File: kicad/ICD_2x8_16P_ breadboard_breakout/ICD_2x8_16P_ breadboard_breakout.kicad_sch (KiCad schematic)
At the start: 3 parts, among them J1 Conn_02x08_Top_Bottom, J2 Conn_01x08, J3 Conn_01x08

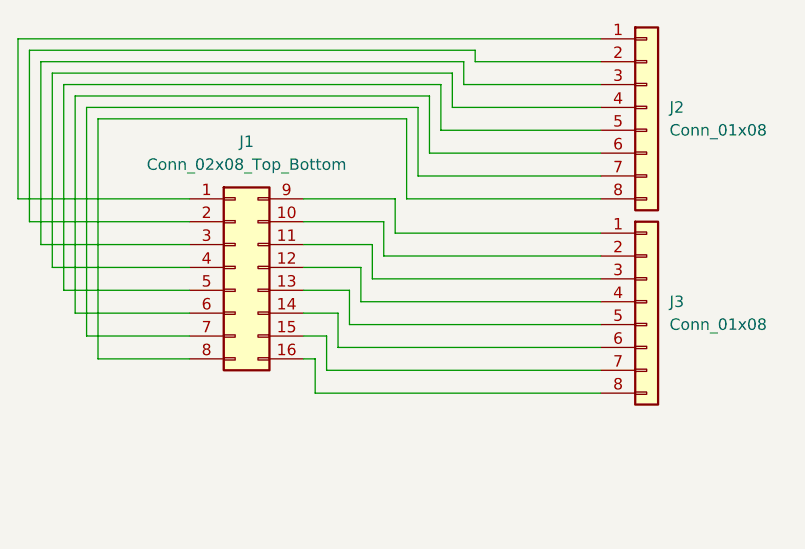
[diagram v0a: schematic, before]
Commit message: Major progress on Serial, KiCAD models, and Python libraries for sensor module base.
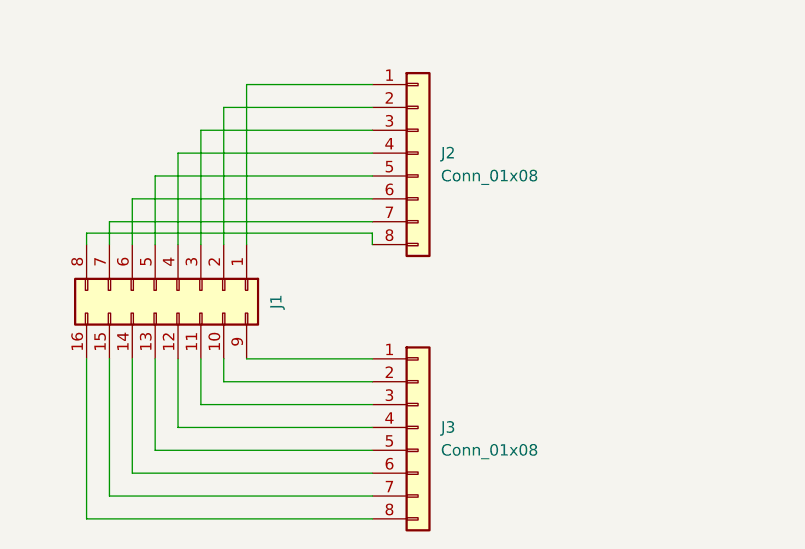
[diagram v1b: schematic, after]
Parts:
- J2, J3: footprint Connector_PinHeader_2.00mm:PinHeader_1x08_P2.00mm_Vertical -> Connector_PinHeader_2.54mm:PinHeader_1x08_P2.54mm_Vertical
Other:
- moved on the sheet: J1, J2, J3
